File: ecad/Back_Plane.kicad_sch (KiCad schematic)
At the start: 0 parts

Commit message: PCB Update
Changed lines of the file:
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@@
 (kicad_sch
-	(version 20231120)
+	(version 20250114)
 	(generator "eeschema")
-	(generator_version "8.0")
+	(generator_version "9.0")
 	(paper "A4")
 	(title_block
@@
 	)
 	(sheet
-		(at 128.27 92.71)
+		(at 54.61 52.07)
 		(size 12.7 3.81)
+		(exclude_from_sim no)
+		(in_bom yes)
+		(on_board yes)
+		(dnp no)
 		(fields_autoplaced yes)
 		(stroke
@@
 		)
 		(property "Sheetname" "Buck_Converter"
-			(at 128.27 91.9984 0)
+			(at 54.61 51.3584 0)
 			(effects
 				(font
@@
 		)
 		(property "Sheetfile" "Power_Distribution.kicad_sch"
-			(at 128.27 97.1046 0)
+			(at 54.61 56.4646 0)
 			(effects
 				(font
@@
 		)
 		(property "Field2" ""
-			(at 128.27 92.71 0)
+			(at 54.61 52.07 0)
 			(effects
 				(font

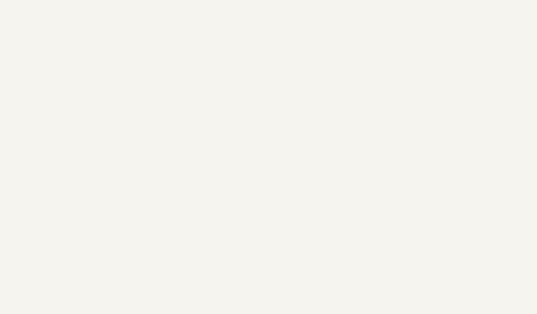
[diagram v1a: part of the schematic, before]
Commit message: Testing Resets Placed
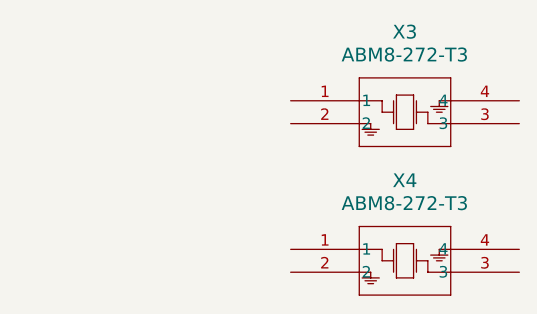
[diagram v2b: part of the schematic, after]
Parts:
- added X3, X4: ABM8-272-T3, ABM8-272-T3_ABR, symbol 2025-02-12_11-47-03:ABM8-272-T3
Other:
- company: (none) -> ECE 477: Digital Systems Design
- title: Buck Converter -> Power Distribution Back Plane
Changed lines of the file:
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@@
 	(paper "A4")
 	(title_block
-		(title "Buck Converter")
+		(title "Power Distribution Back Plane")
+		(date "2025-02-26")
+		(company "ECE 477: Digital Systems Design")
 		(comment 1 "Brian Lu")
 		(comment 2 "Nathan Huang")
@@
 		(comment 4 "Seth Deegan")
 	)
+	(symbol
+		(lib_id "2025-02-12_11-47-03:ABM8-272-T3")
+		(at 120.65 58.42 0)
+		(unit 1)
+		(exclude_from_sim no)
+		(in_bom yes)
+		(on_board yes)
+		(dnp no)
+		(fields_autoplaced yes)
+		(property "Reference" "X3"
+			(at 133.35 50.8 0)
+			(effects
+				(font
+					(size 1.524 1.524)
+				)
+			)
+		)
+		(property "Value" "ABM8-272-T3"
+			(at 133.35 53.34 0)
+			(effects
+				(font
+					(size 1.524 1.524)
+				)
+			)
+		)
+		(property "Footprint" "ABM8-272-T3_ABR"
+			(at 120.904 55.88 0)
+			(effects
+				(font
+					(size 1.27 1.27)
+					(italic yes)
+				)
+				(hide yes)
+			)
+		)
+		(property "Datasheet" "ABM8-272-T3"
+			(at 118.618 54.102 0)
+			(effects
+				(font
+					(size 1.27 1.27)
+					(italic yes)
+				)
+				(hide yes)
+			)
+		)
+		(property "Description" ""
+			(at 120.65 58.42 0)
+			(effects
+				(font
+					(size 1.27 1.27)
+				)
+				(hide yes)
+			)
+		)
+		(pin "2"
+		)
+		(pin "1"
+		)
+		(pin "4"
+		)
+		(pin "3"
+		)
+		(instances
+			(project ""
+				(path "/b682b302-8ca4-4b40-b0cb-fd99f4675538/8ac99590-cdb7-457f-9b2c-c22421ccb183"
+					(reference "X3")
+					(unit 1)
+				)
+			)
+		)
+	)
+	(symbol
+		(lib_id "2025-02-12_11-47-03:ABM8-272-T3")
+		(at 120.65 74.93 0)
+		(unit 1)
+		(exclude_from_sim no)
+		(in_bom yes)
+		(on_board yes)
+		(dnp no)
+		(fields_autoplaced yes)
+		(property "Reference" "X4"
+			(at 133.35 67.31 0)
+			(effects
+				(font
+					(size 1.524 1.524)
+				)
+			)
+		)
+		(property "Value" "ABM8-272-T3"
+			(at 133.35 69.85 0)
+			(effects
+				(font
+					(size 1.524 1.524)
+				)
+			)
+		)
+		(property "Footprint" "ABM8-272-T3_ABR"
+			(at 120.904 72.39 0)
+			(effects
+				(font
+					(size 1.27 1.27)
+					(italic yes)
+				)
+				(hide yes)
+			)
+		)
+		(property "Datasheet" "ABM8-272-T3"
+			(at 118.618 70.612 0)
+			(effects
+				(font
+					(size 1.27 1.27)
+					(italic yes)
+				)
+				(hide yes)
+			)
+		)
+		(property "Description" ""
+			(at 120.65 74.93 0)
+			(effects
+				(font
+					(size 1.27 1.27)
+				)
+				(hide yes)
+			)
+		)
+		(pin "2"
+		)
+		(pin "1"
+		)
+		(pin "4"
+		)
+		(pin "3"
+		)
+		(instances
+			(project "ecad"
+				(path "/b682b302-8ca4-4b40-b0cb-fd99f4675538/8ac99590-cdb7-457f-9b2c-c22421ccb183"
+					(reference "X4")
+					(unit 1)
+				)
+			)
+		)
+	)
 	(sheet

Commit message: Ready for Layout
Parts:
- removed X3, X4: ABM8-272-T3, ABM8-272-T3_ABR, symbol 2025-02-12_11-47-03:ABM8-272-T3
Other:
- note added: "DIM SLOTS"
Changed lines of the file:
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@@
 		(comment 4 "Seth Deegan")
 	)
-	(symbol
-		(lib_id "2025-02-12_11-47-03:ABM8-272-T3")
-		(at 120.65 58.42 0)
-		(unit 1)
-		(exclude_from_sim no)
-		(in_bom yes)
-		(on_board yes)
-		(dnp no)
-		(fields_autoplaced yes)
-		(property "Reference" "X3"
-			(at 133.35 50.8 0)
-			(effects
-				(font
-					(size 1.524 1.524)
-				)
-			)
+	(rectangle
+		(start 22.86 30.48)
+		(end 111.76 115.57)
+		(stroke
+			(width 0)
+			(type default)
 		)
-		(property "Value" "ABM8-272-T3"
-			(at 133.35 53.34 0)
-			(effects
-				(font
-					(size 1.524 1.524)
-				)
-			)
-		)
-		(property "Footprint" "ABM8-272-T3_ABR"
-			(at 120.904 55.88 0)
-			(effects
-				(font
-					(size 1.27 1.27)
-					(italic yes)
-				)
-				(hide yes)
-			)
-		)
-		(property "Datasheet" "ABM8-272-T3"
-			(at 118.618 54.102 0)
-			(effects
-				(font
-					(size 1.27 1.27)
-					(italic yes)
-				)
-				(hide yes)
-			)
-		)
-		(property "Description" ""
-			(at 120.65 58.42 0)
-			(effects
-				(font
-					(size 1.27 1.27)
-				)
-				(hide yes)
-			)
-		)
-		(pin "2"
-		)
-		(pin "1"
-		)
-		(pin "4"
-		)
-		(pin "3"
-		)
-		(instances
-			(project ""
-				(path "/b682b302-8ca4-4b40-b0cb-fd99f4675538/8ac99590-cdb7-457f-9b2c-c22421ccb183"
-					(reference "X3")
-					(unit 1)
-				)
-			)
+		(fill
+			(type none)
 		)
 	)
-	(symbol
-		(lib_id "2025-02-12_11-47-03:ABM8-272-T3")
-		(at 120.65 74.93 0)
-		(unit 1)
+	(text "DIM SLOTS"
 		(exclude_from_sim no)
-		(in_bom yes)
-		(on_board yes)
-		(dnp no)
-		(fields_autoplaced yes)
-		(property "Reference" "X4"
-			(at 133.35 67.31 0)
-			(effects
-				(font
-					(size 1.524 1.524)
-				)
-			)
-		)
-		(property "Value" "ABM8-272-T3"
-			(at 133.35 69.85 0)
-			(effects
-				(font
-					(size 1.524 1.524)
-				)
-			)
-		)
-		(property "Footprint" "ABM8-272-T3_ABR"
-			(at 120.904 72.39 0)
-			(effects
-				(font
-					(size 1.27 1.27)
-					(italic yes)
-				)
-				(hide yes)
-			)
-		)
-		(property "Datasheet" "ABM8-272-T3"
-			(at 118.618 70.612 0)
-			(effects
-				(font
-					(size 1.27 1.27)
-					(italic yes)
-				)
-				(hide yes)
-			)
-		)
-		(property "Description" ""
-			(at 120.65 74.93 0)
-			(effects
-				(font
-					(size 1.27 1.27)
-				)
-				(hide yes)
-			)
-		)
-		(pin "2"
-		)
-		(pin "1"
-		)
-		(pin "4"
-		)
-		(pin "3"
-		)
-		(instances
-			(project "ecad"
-				(path "/b682b302-8ca4-4b40-b0cb-fd99f4675538/8ac99590-cdb7-457f-9b2c-c22421ccb183"
-					(reference "X4")
-					(unit 1)
-				)
+		(at 30.48 29.21 0)
+		(effects
+			(font
+				(size 1.27 1.27)
 			)
 		)
 	)
 	(sheet
-		(at 54.61 52.07)
+		(at 121.92 34.29)
 		(size 12.7 3.81)
 		(exclude_from_sim no)
@@
 		)
 		(property "Sheetname" "Buck_Converter"
-			(at 54.61 51.3584 0)
+			(at 121.92 33.5784 0)
 			(effects
 				(font
@@
 		)
 		(property "Sheetfile" "Power_Distribution.kicad_sch"
-			(at 54.61 56.4646 0)
+			(at 121.92 38.6846 0)
 			(effects
 				(font
@@
 		)
 		(property "Field2" ""
-			(at 54.61 52.07 0)
+			(at 121.92 34.29 0)
 			(effects
 				(font
@@
 			(project "ecad"
 				(path "/b682b302-8ca4-4b40-b0cb-fd99f4675538/8ac99590-cdb7-457f-9b2c-c22421ccb183"
-					(page "2")
+					(page "3")
 				)
 			)

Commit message: Back Plane Nearly Complete
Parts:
- added J5: 10145226-0241N13LF, 10145226-0241N13LF:AMPHENOL_10145226-0241N13LF, symbol 10145226-0241N13LF:10145226-0241N13LF
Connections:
- new net 3.3V: J5.10, J5.124, J5.125, J5.153, J5.154, J5.165, J5.166, J5.177, J5.178, J5.189, J5.190, J5.197, J5.198, J5.209, J5.21, J5.210, J5.22, J5.236, J5.237, J5.276, J5.33, J5.34, J5.45, J5.46, J5.53, J5.54, J5.65, J5.66, J5.9, J5.98, J5.99
- new net ADDR00: J5.1, J5.145
- new net ADDR01: J5.146, J5.2
- new net ADDR02: J5.147, J5.3
- new net ADDR03: J5.148, J5.4
- new net ADDR04: J5.149, J5.5
- new net ADDR05: J5.150, J5.6
- new net ADDR06: J5.151, J5.7
- new net ADDR07: J5.152, J5.164, J5.20, J5.8
- new net ADDR08: J5.13, J5.157
- new net ADDR09: J5.14, J5.158
- new net ADDR10: J5.15, J5.159
- new net ADDR11: J5.16, J5.160
- new net ADDR12: J5.161, J5.17
- new net ADDR13: J5.162, J5.18
- new net ADDR14: J5.163, J5.19
- new net BUS00: J5.169, J5.25
- new net BUS01: J5.170, J5.26
- new net BUS02: J5.171, J5.27
- new net BUS03: J5.172, J5.28
- new net BUS04: J5.173, J5.29
- new net BUS05: J5.174, J5.30
- new net BUS06: J5.175, J5.31
- new net BUS07: J5.176, J5.32
- new net BUS08: J5.181, J5.37
- new net BUS09: J5.182, J5.38
- new net BUS10: J5.183, J5.39
- new net BUS11: J5.184, J5.40
- new net BUS12: J5.185, J5.41
- new net BUS13: J5.186, J5.42
- new net BUS14: J5.187, J5.43
- new net BUS15: J5.188, J5.44
- new net BUS16: J5.193, J5.49
- new net BUS17: J5.194, J5.50
- new net BUS18: J5.195, J5.51
- new net BUS19: J5.196, J5.52
- new net DATA0: J5.201, J5.57
- new net DATA1: J5.202, J5.58
- new net DATA2: J5.203, J5.59
- new net DATA3: J5.204, J5.60
- new net DATA4: J5.205, J5.61
- new net DATA5: J5.206, J5.62
- new net DATA6: J5.207, J5.63
- new net DATA7: J5.208, J5.64
- new net GND: J5.100, J5.101, J5.11, J5.12, J5.126, J5.127, J5.155, J5.156, J5.167, J5.168, J5.179, J5.180, J5.191, J5.192, J5.199, J5.200, J5.211, J5.212, J5.23, J5.238, J5.239, J5.24, J5.278, J5.35, J5.36, J5.47, J5.48, J5.55, J5.56, J5.67, J5.68
- no-connect marks 0 -> 138
